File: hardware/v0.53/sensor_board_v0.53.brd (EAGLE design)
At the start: 55.2 x 39.9 mm, 51 parts, among them J3 USB-MICROB, U1 ATMEGA328P, U3 OPA344, U4 RFM69HW, U5 FT231XS, U6 ADMP401, U7 SHT31-DIS, U8 MCP1703CB, U9 BMP280, Y1 16MHZ

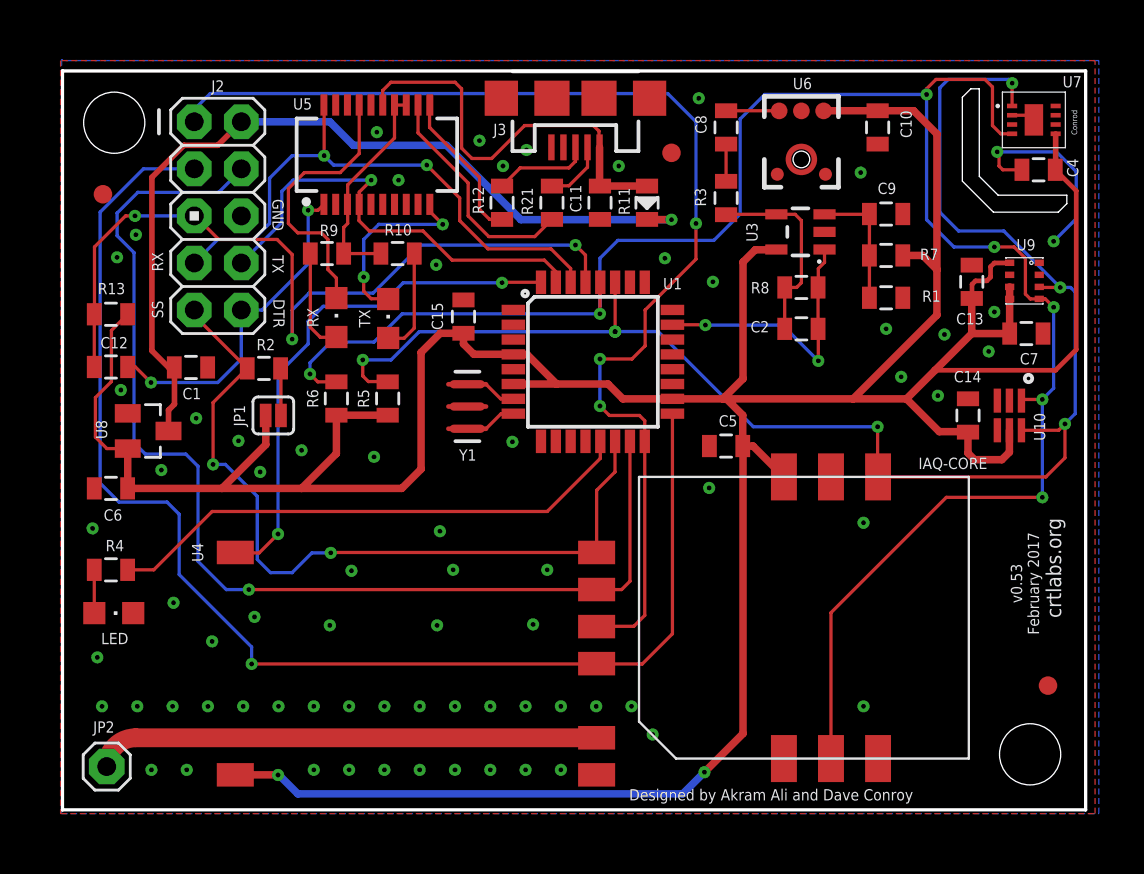
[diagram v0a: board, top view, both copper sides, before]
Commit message: Update - Features added
- Replaced regular LED with RGB LED (NeoPixel from Adafruit)
- Adjusted overall dimensions to give slightly higher tolerance for mounting holes
- I2C pins broken out to headers
- Two digital pins broken out (for software serial)
- Extra power pins broken out (for powering external devices or connecting ground)
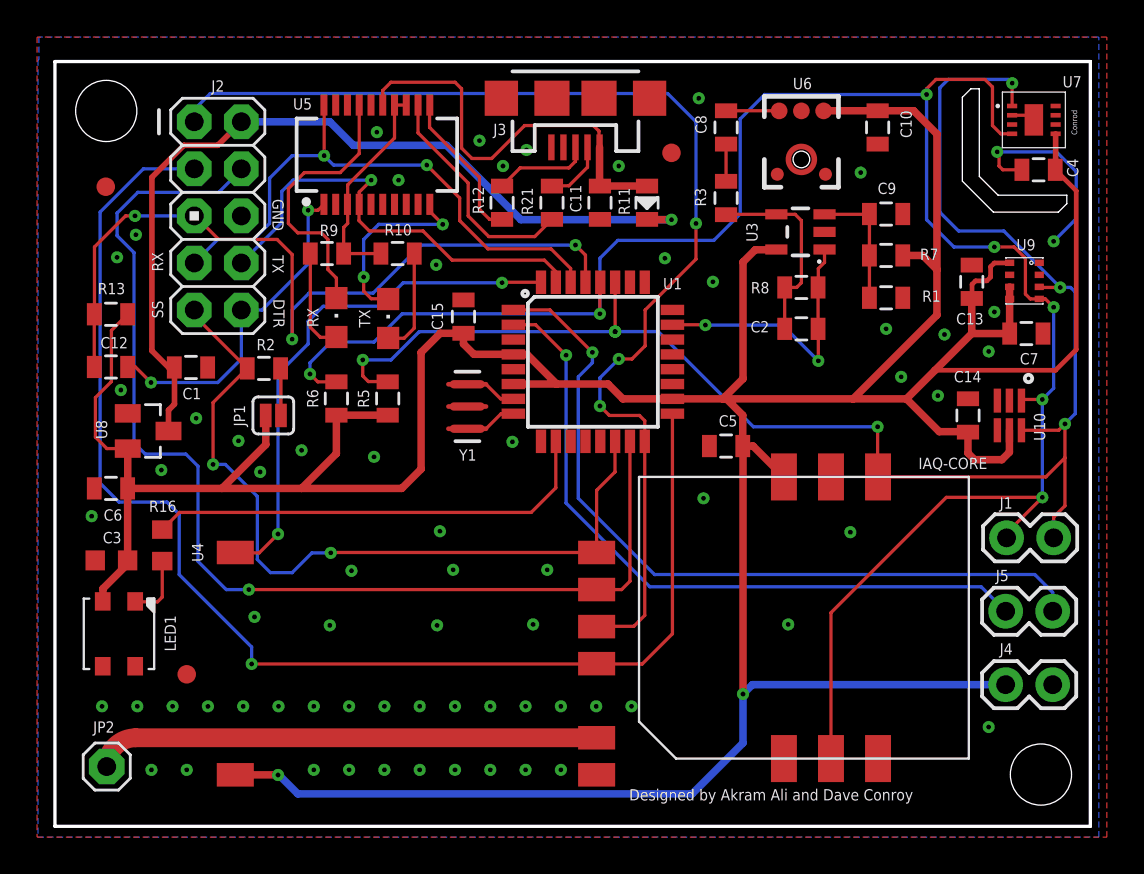
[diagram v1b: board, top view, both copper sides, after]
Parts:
- removed LED: (no value), adafruit:CHIPLED_0805
- removed R4: 47, SparkFun-Resistors:0805
- added C3: 1uF, adafruit:C0603K
- added J1, J4, J5: (no value), SparkFun-Connectors:1X02
- added LED1: WS2812B3535, adafruit:LED3535
- added R16: 470, adafruit:R0603
- U10: value (none) -> TSL2591
- moved U$1 46.5 mm to (8.38, 13.9)
- moved H2 1.24 mm to (54.5, 8.51)
- moved H1 0.77 mm to (4.04, 44.3)
- moved U$2 0.43 mm to (4.01, 40.2)
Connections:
- removed net N$2: R4.1, U1.13
- removed net N$3: LED.A, R4.2
- new net D3: J5.2, U1.1
- new net D4: J5.1, U1.2
- new net D6: R16.2, U1.10
- new net N$7: LED1.1, R16.1
- net GND: now also C3.2, J4.1, LED1.4; no longer LED.C
- net SCL: now also J1.1
- net SDA: now also J1.2
- net VCC: now also C3.1, J4.2, LED1.2
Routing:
- net D3: track 0.00 -> 42.1 mm, vias 0 -> 1
- net D4: track 0.00 -> 37.6 mm, vias 0 -> 1
- net N$2: track 28.9 -> 0.00 mm
- net D6: track 0.00 -> 24.7 mm
- net VCC: track 207.0 -> 228.3 mm
- net SDA: track 82.8 -> 87.4 mm
- net N$7: track 0.00 -> 3.52 mm
- net SCL: track 105.7 -> 108.7 mm
- net N$3: track 2.34 -> 0.00 mm
- net MISO: track 63.3 -> 62.7 mm
- net GND: vias 71 -> 68
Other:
- board size 55.2 x 39.9 mm -> 55.9 x 41.3 mm
- board text added: "v0.53 | March 2017"
- board text removed: "v0.53 February 2017"

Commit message: Trace adjustments
Moved the radio and IAQ Core a bit to the left to allow more space for headers
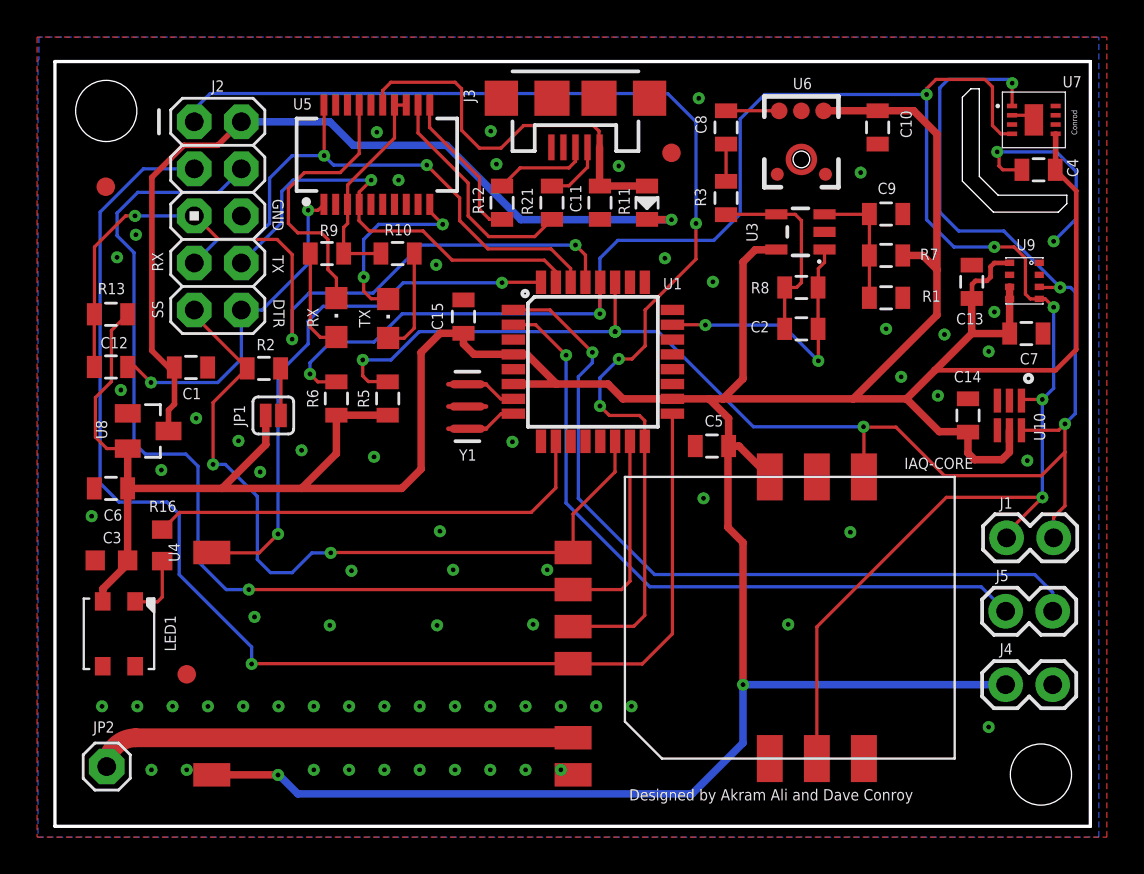
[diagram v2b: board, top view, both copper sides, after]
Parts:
- moved U4 1.27 mm to (21.2, 15.5)
- moved C5 0.76 mm to (36.7, 26.2)
- moved IAQ-CORE 0.76 mm to (32.0, 9.37)
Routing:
- net VCC: track 228.3 -> 229.7 mm
- net D2: track 28.3 -> 29.6 mm
- net ANT: track 27.1 -> 25.8 mm
- net MISO: track 62.7 -> 64.0 mm
- net SDA: track 87.4 -> 88.6 mm
- net VBUS: track 22.6 -> 21.6 mm
- net SS: track 42.3 -> 41.5 mm

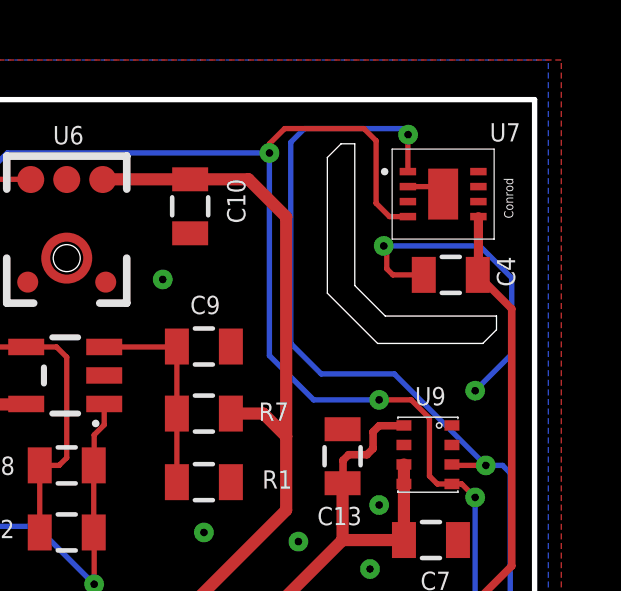
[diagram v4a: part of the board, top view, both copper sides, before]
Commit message: Updated SHT31/35 library
Replaced old library with Adafruit version - slightly longer pads to avoid potential bridging during reflow.
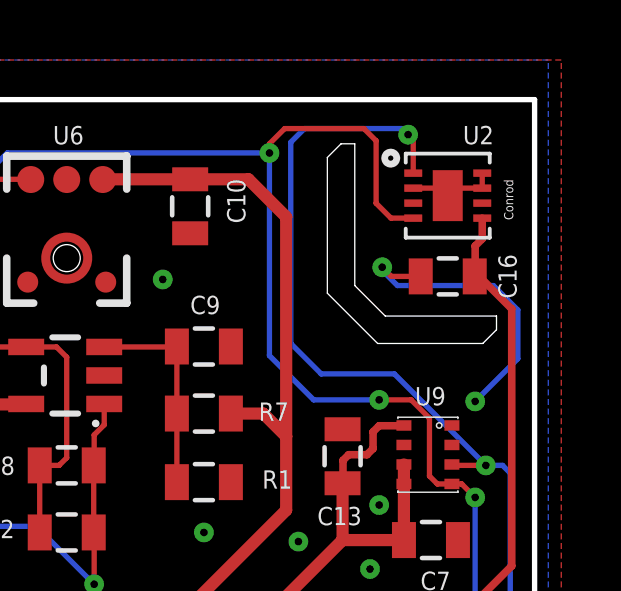
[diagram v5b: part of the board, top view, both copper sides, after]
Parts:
- removed C4: 0.1uF, SparkFun-Passives:0805
- removed U7: SHT31-DIS, thomasb9511:SHT3X
- added C16: 0.1uF, SparkFun-Passives:0805
- added U2: (no value), Adafruit SHT31:SHT3X
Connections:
- net GND: now also C16.2, U2.2, U2.7, U2.8, U2.THERMAL; no longer C4.2, U7.P$2, U7.P$7, U7.P$8, U7.PAD
- net SCL: now also U2.4; no longer U7.P$4
- net SDA: now also U2.1; no longer U7.P$1
- net VCC: now also C16.1, U2.5; no longer C4.1, U7.P$5
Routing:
- net GND: track 12.4 -> 13.2 mm

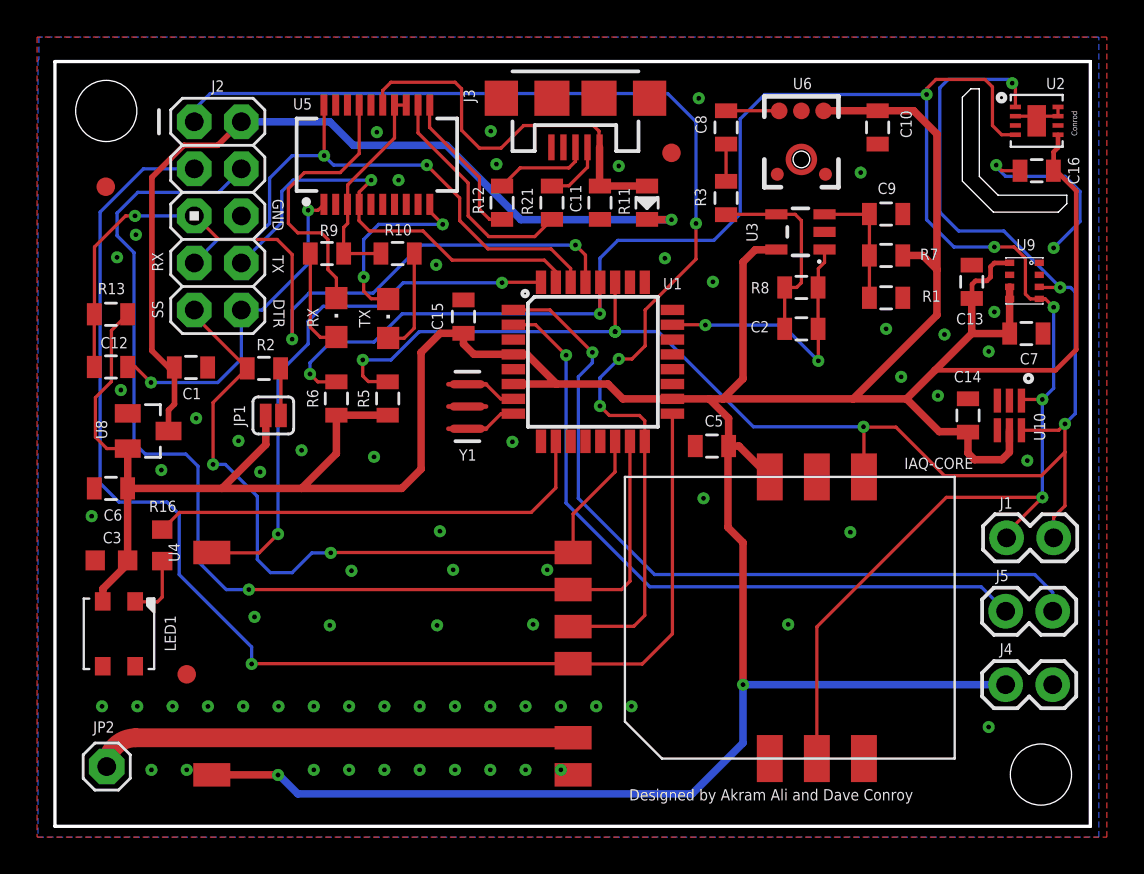
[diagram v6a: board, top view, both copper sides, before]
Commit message: v0.53 - update
- Aligned light sensor with RGB LED
- Moved jumpers location after moving light sensor
- Added PM2.5 jumpers (RX/TX/PWR/GND)
- Adjusted some passive components
- Several trace adjustments
- Slightly increased board dimensions for added tolerance on mounting
holes
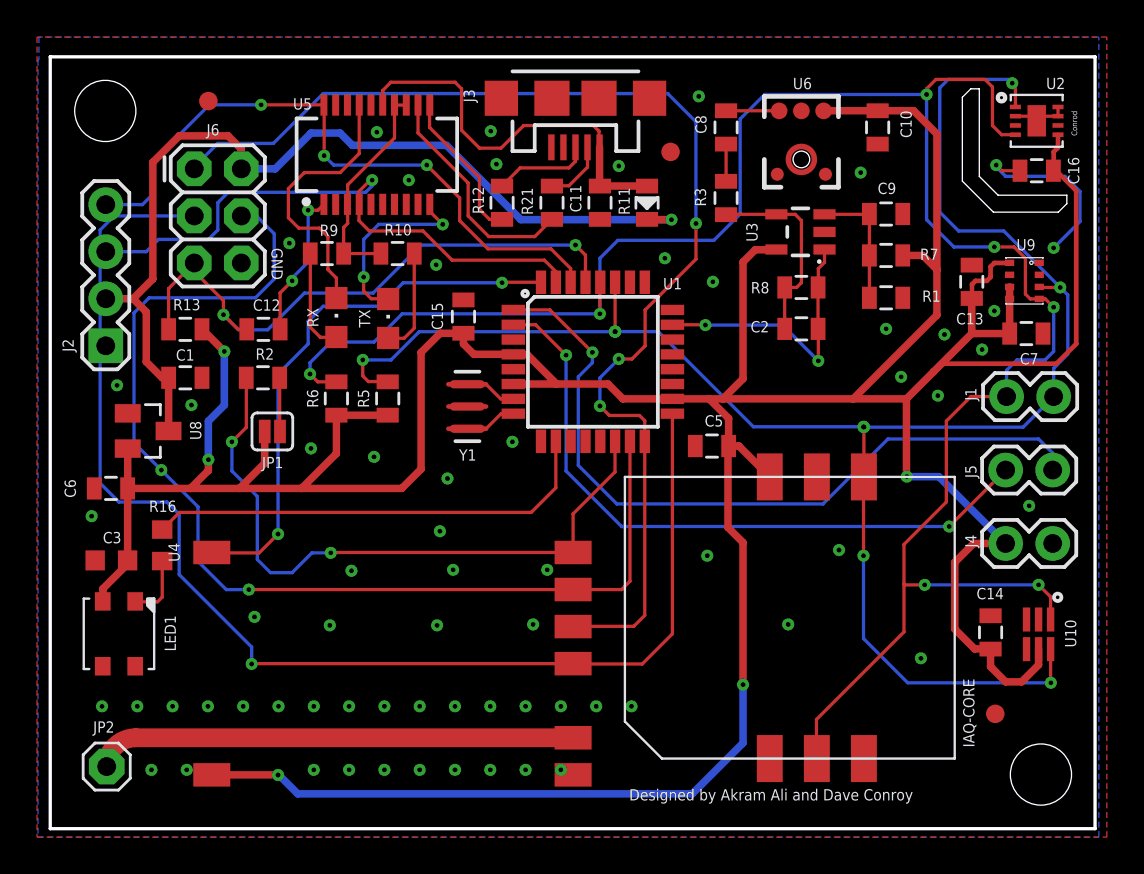
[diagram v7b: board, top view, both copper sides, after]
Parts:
- added J6: AVR_SPI_PRG_6PTH, SparkFun-Connectors:2X3
- J2: device SparkFun-Connectors:AVR_ICSP -> SparkFun-Connectors:1X04
- moved U$2 55.8 mm to (52.0, 11.8)
- moved U$1 31.0 mm to (9.55, 44.9)
- moved U10 11.9 mm to (54.4, 16.1)
- moved C14 11.8 mm to (51.8, 16.2)
- moved J2 9.26 mm to (4.01, 31.6), turned to 90 degrees
- moved C12 8.48 mm to (12.5, 32.5)
- moved J1 7.62 mm to (52.6, 28.9)
- moved J4 7.62 mm to (55.1, 21.0)
- moved J5 7.62 mm to (52.6, 24.9)
- moved R13 4.09 mm to (8.31, 32.5)
- moved JP1 0.87 mm to (13.0, 27.0)
- moved C1 0.64 mm to (8.31, 29.9)
- moved R2 0.51 mm to (12.5, 29.9)
- moved U$3 0.07 mm to (34.5, 42.1)
- moved H1 0.05 mm to (3.99, 44.3)
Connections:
- net DTR: no longer J2.10
- net GND: now also J2.1, J6.6; no longer J2.6
- net MISO: now also J6.1; no longer J2.1
- net MOSI: now also J6.4; no longer J2.4
- net PWR: now also J6.2
- net RESET: now also J6.5; no longer J2.5
- net RX: now also J2.4; no longer J2.7
- net SCK: now also J6.3; no longer J2.3
- net SS: no longer J2.9
- net TX: now also J2.3; no longer J2.8
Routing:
- net RESET: track 43.8 -> 32.7 mm, vias 3 -> 2
- net DTR: track 18.2 -> 8.04 mm
- net SDA: track 88.7 -> 98.0 mm, vias 7 -> 9
- net TX: track 24.6 -> 31.9 mm
- net SS: track 41.5 -> 35.4 mm
- net SCL: track 109.2 -> 113.5 mm
- net RX: track 30.9 -> 35.1 mm, vias 2 -> 3
- net PWR: track 47.3 -> 51.4 mm
- net MOSI: track 61.3 -> 59.5 mm
- net D4: track 37.6 -> 36.0 mm, vias 1 -> 2
- net SCK: track 70.6 -> 69.0 mm
- net D3: track 42.1 -> 40.8 mm
- net VCC: track 229.8 -> 231.2 mm, vias 2 -> 5
- net MISO: track 64.0 -> 64.7 mm
- net GND: vias 68 -> 66
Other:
- board size 55.9 x 41.3 mm -> 56.4 x 41.7 mm
- board text removed: "DTR"
- board text removed: "RX"
- board text removed: "SS"
- board text removed: "TX"

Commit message: v0.53 - update
- (previous commit: Replaced 10-pin header with 6-pin ISP header)
- This commit: Added 1K resistors in series with FTDI's RX/TX line to
give priority to external serial devices (unplug external device to
program the board)
- Some trace/silkscreen adjustments
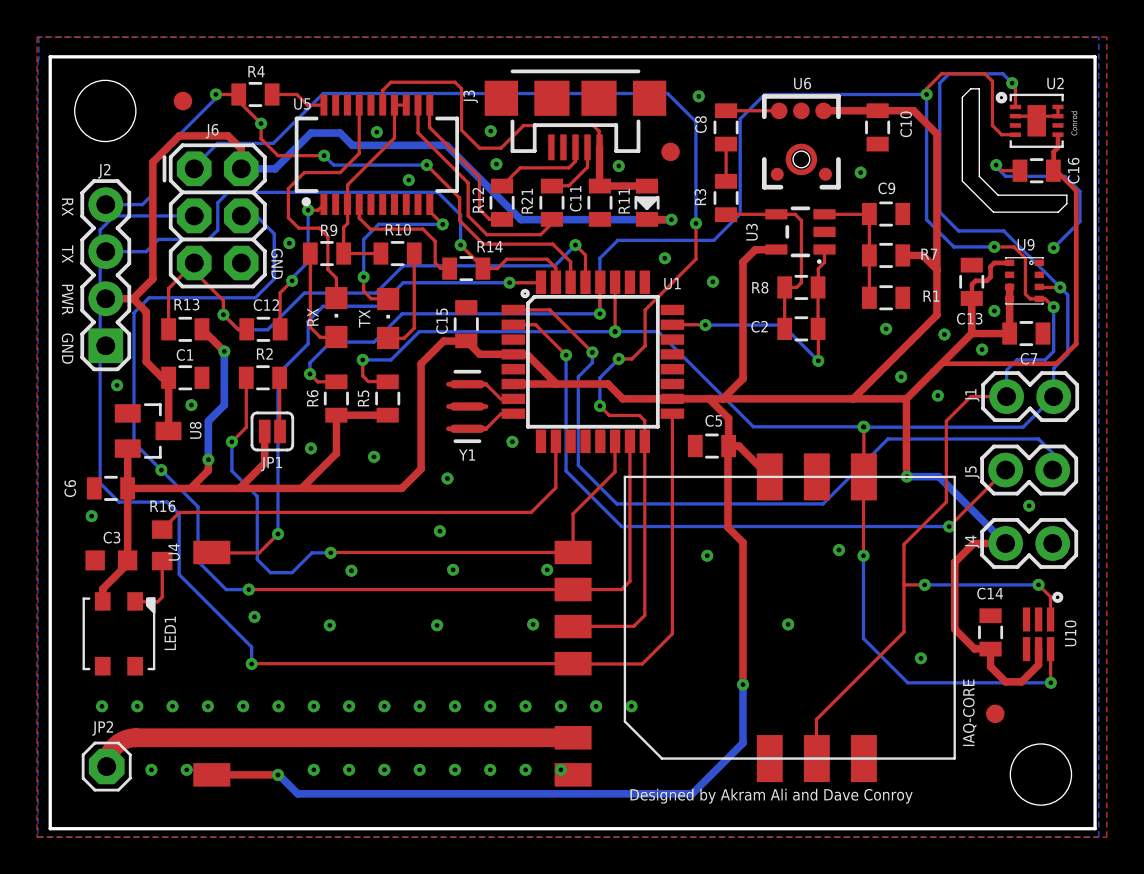
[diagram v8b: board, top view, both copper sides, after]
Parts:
- added R14, R4: 10K, SparkFun-Passives:0805
- moved U$1 1.37 mm to (8.18, 44.9)
- moved C15 0.43 mm to (23.5, 32.8)
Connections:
- new net N$2: R14.2, U5.4
- new net N$3: R4.2, U5.20
- net RX: now also R4.1; no longer U5.20
- net TX: now also R14.1; no longer U5.4
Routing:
- net N$2: track 0.00 -> 7.43 mm
- net N$3: track 0.00 -> 3.03 mm
- net TX: track 31.9 -> 30.4 mm
- net VCC: track 231.2 -> 230.2 mm
- net SDA: track 98.0 -> 98.7 mm
- net RX: track 35.1 -> 35.0 mm, vias 3 -> 4
- net GND: vias 66 -> 65
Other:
- board text added: "PWR"
- board text added: "RX"
- board text added: "TX"
